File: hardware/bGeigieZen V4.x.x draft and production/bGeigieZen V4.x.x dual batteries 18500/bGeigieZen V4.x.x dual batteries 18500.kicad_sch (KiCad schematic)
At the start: 14 parts, among them J1 M5 2x15 pin, J11 QI input +5V, J2 Geiger IRover, J3 GPS, J4 Geiger Safepulse, J5 Extra support header, J6 Grove, J7 QI GND out, J8 QI input GND, J9 QI battery out

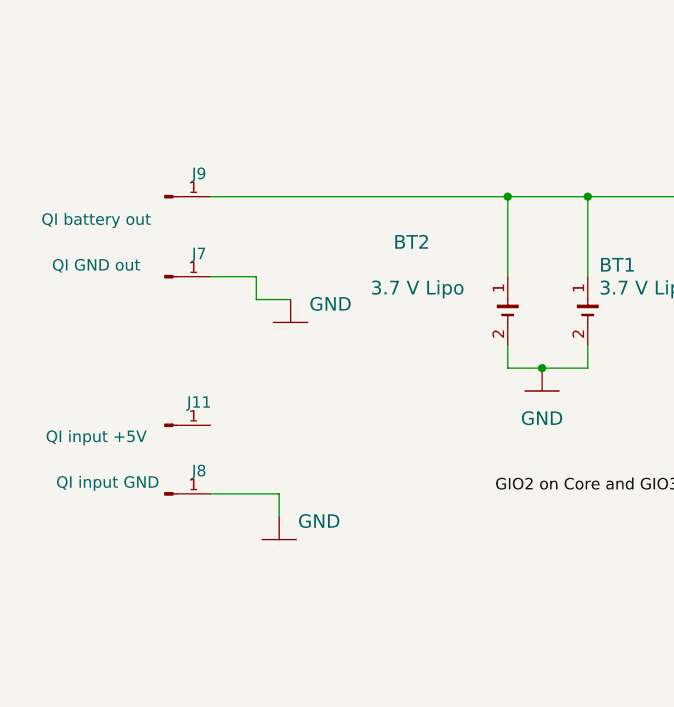
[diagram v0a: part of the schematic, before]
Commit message: Updated dual 18500 V4.x.x boards
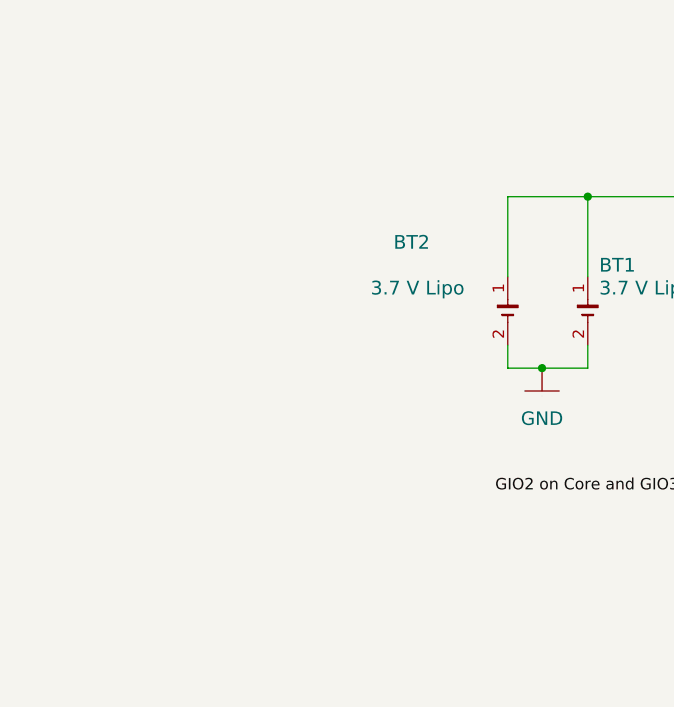
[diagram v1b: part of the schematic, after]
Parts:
- removed J11: QI input +5V, Connector_PinHeader_2.54mm:PinHeader_1x01_P2.54mm_Vertical, symbol Connector:Conn_01x01_Pin
- removed J7: QI GND out, Connector_PinHeader_2.54mm:PinHeader_1x01_P2.54mm_Vertical, symbol Connector:Conn_01x01_Pin
- removed J8: QI input GND, Connector_PinHeader_2.54mm:PinHeader_1x01_P2.54mm_Vertical, symbol Connector:Conn_01x01_Pin
- removed J9: QI battery out, Connector_PinHeader_2.54mm:PinHeader_1x01_P2.54mm_Vertical, symbol Connector:Conn_01x01_Pin

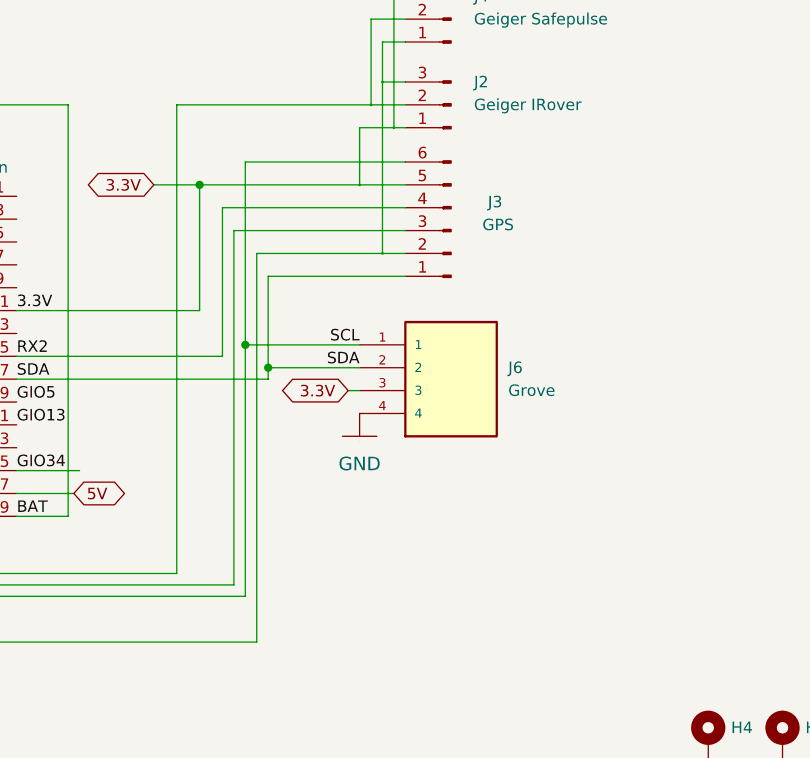
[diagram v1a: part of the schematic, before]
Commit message: Updated  boards to V4.0.4
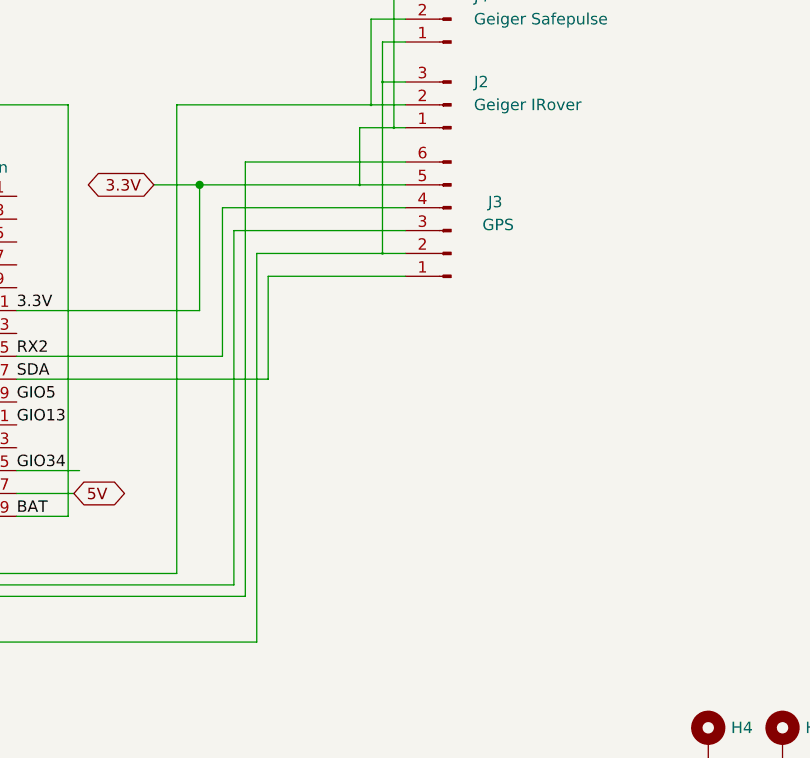
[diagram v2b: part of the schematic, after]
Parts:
- removed J6: Grove, Connector_PinSocket_2.00mm:PinSocket_1x04_P2.00mm_Horizontal, symbol 110990030:110990030
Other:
- title: bGeigieZen V4.0.3 -> bGeigieZen V4.0.4

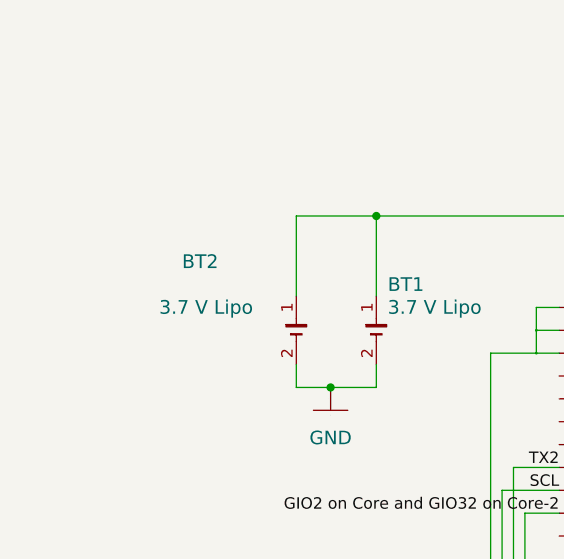
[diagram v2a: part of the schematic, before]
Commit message: Added LiPo charger connector
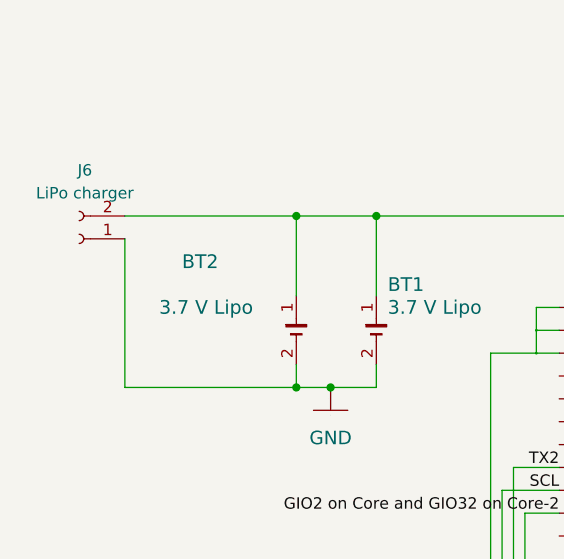
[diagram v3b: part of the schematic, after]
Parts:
- added J6: LiPo charger, Connector_JST:JST_PH_B2B-PH-K_1x02_P2.00mm_Vertical, symbol Connector:Conn_01x02_Socket
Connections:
- net BAT: now also J6.2 (Pin_2)
- net GND: now also J6.1 (Pin_1)
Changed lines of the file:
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@@
+	)
+	(junction
+		(at 104.14 66.04)
+		(diameter 0)
+		(color 0 0 0 0)
+	)
+	(junction
+		(at 104.14 85.09)
+		(diameter 0)
+		(color 0 0 0 0)
 	)
 	(junction
@@
 	(wire
 		(pts
+			(xy 104.14 85.09) (xy 107.95 85.09)
+		)
+		(stroke
+			(width 0)
+			(type default)
+		)
+	)
+	(wire
+		(pts
 			(xy 133.35 104.14) (xy 131.445 104.14)
 		)
@@
 	(wire
 		(pts
+			(xy 85.09 68.58) (xy 85.09 85.09)
+		)
+		(stroke
+			(width 0)
+			(type default)
+		)
+	)
+	(wire
+		(pts
 			(xy 171.45 72.39) (xy 189.23 72.39)
 		)
@@
 	(wire
 		(pts
-			(xy 104.14 85.09) (xy 107.95 85.09)
+			(xy 85.09 85.09) (xy 104.14 85.09)
 		)
 		(stroke
@@
 			(width 0)
 			(type solid)
+		)
+	)
+	(wire
+		(pts
+			(xy 85.09 66.04) (xy 104.14 66.04)
+		)
+		(stroke
+			(width 0)
+			(type default)
 		)
 	)
@@
 					(unit 1)
 				)
+			)
+		)
+	)
+	(symbol
+		(lib_id "Connector:Conn_01x02_Socket")
+		(at 80.01 68.58 180)
+		(unit 1)
+		(exclude_from_sim no)
+		(in_bom yes)
+		(on_board yes)
+		(dnp no)
+		(fields_autoplaced yes)
+		(property "Reference" "J6"
+			(at 80.645 60.96 0)
+			(effects
+				(font
+					(size 1.27 1.27)
+				)
+			)
+		)
+		(property "Value" "LiPo charger"
+			(at 80.645 63.5 0)
+			(effects
+				(font
+					(size 1.27 1.27)
+				)
+			)
+		)
+		(property "Footprint" "Connector_JST:JST_PH_B2B-PH-K_1x02_P2.00mm_Vertical"
+			(at 80.01 68.58 0)
+			(effects
+				(font
+					(size 1.27 1.27)
+				)
+				(hide yes)
+			)
+		)
+		(property "Datasheet" "~"
+			(at 80.01 68.58 0)
+			(effects
+				(font
+					(size 1.27 1.27)
+				)
+				(hide yes)
+			)
+		)
+		(property "Description" "Generic connector, single row, 01x02, script generated"
+			(at 80.01 68.58 0)
+			(effects
+				(font
+					(size 1.27 1.27)
+				)
+				(hide yes)
+			)
+		)
+		(pin "2"
+		)
+		(pin "1"
+		)
+		(instances
+			(project ""
+				(path "/c2e3a215-6a49-419d-95d1-595f35b17280"
+					(reference "J6")
+					(unit 1)
+				)
